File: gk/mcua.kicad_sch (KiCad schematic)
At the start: 16 parts, among them SW1 SW_Push, SW2 SW_Push, U4 STM32H747BITx, Y1 16MHz

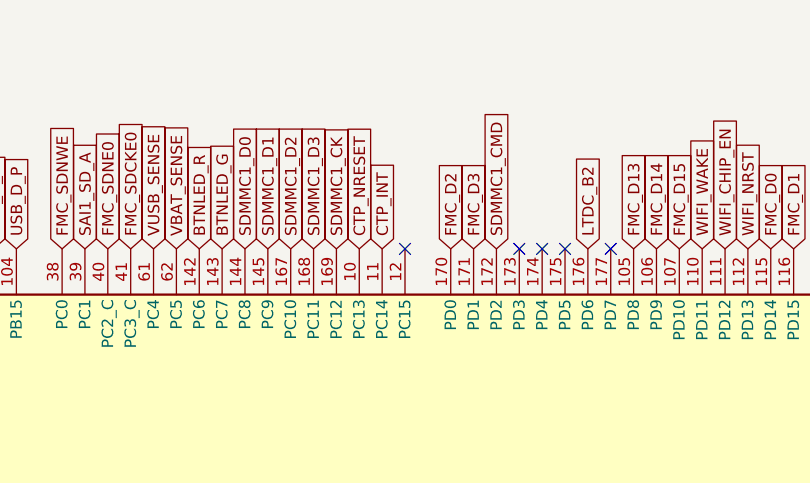
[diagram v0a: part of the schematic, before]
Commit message: Add SD power switch
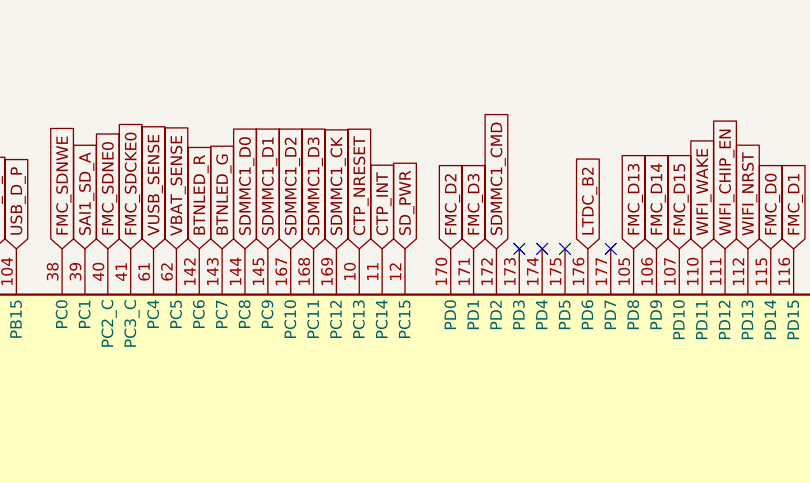
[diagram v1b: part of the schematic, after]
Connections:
- net SD_PWR: now reaches U4.12 (PC15)
- no-connect marks 20 -> 19
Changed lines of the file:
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@@
   (no_connect (at 66.04 49.53))
   (no_connect (at 35.56 49.53))
+  (no_connect (at 73.66 49.53))
   (no_connect (at 165.1 146.05))
   (no_connect (at 63.5 146.05))
   (no_connect (at 66.04 146.05))
   (no_connect (at 50.8 146.05))
-  (no_connect (at 160.02 49.53))
   (no_connect (at 86.36 146.05))
   (no_connect (at 73.66 146.05))
-  (no_connect (at 73.66 49.53))
   (no_connect (at 58.42 49.53))
   (no_connect (at 60.96 146.05))
@@
       (effects (font (size 1.27 1.27)) (justify left) hide)
     )
+  )
+  (global_label "SD_PWR" (shape input) (at 160.02 49.53 90) (fields_autoplaced)
+    (effects (font (size 1.27 1.27)) (justify left))
+    (property "Intersheetrefs" "${INTERSHEET_REFS}" (at 160.02 39.1063 90)
+      (effects (font (size 1.27 1.27)) (justify left) hide)
+    )

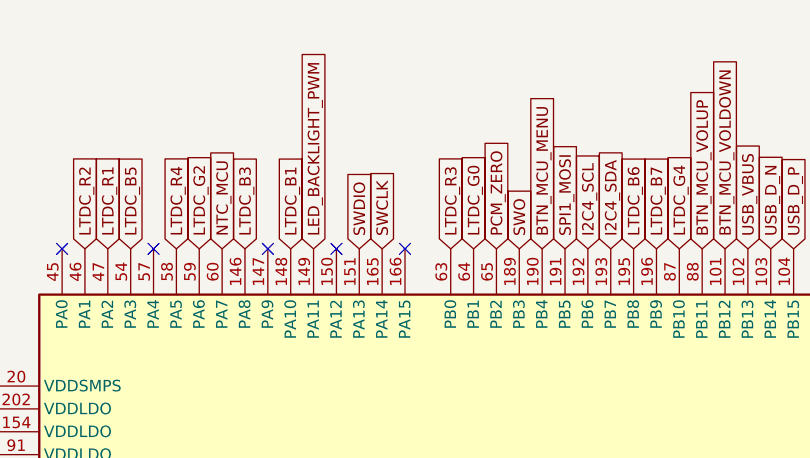
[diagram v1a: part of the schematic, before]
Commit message: update power button routing
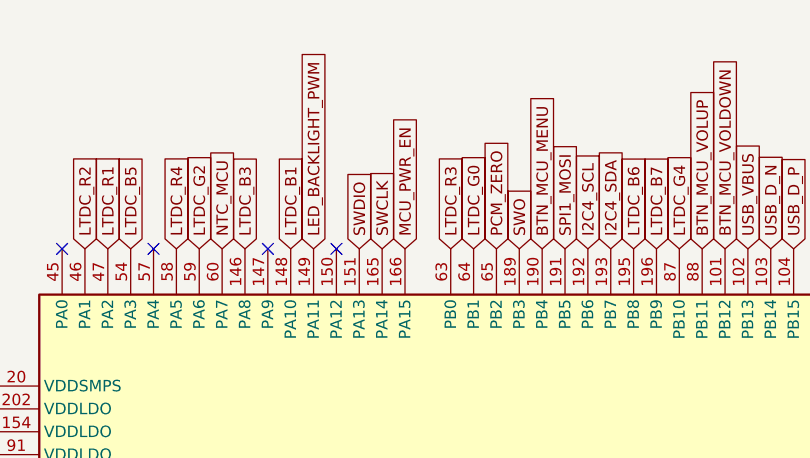
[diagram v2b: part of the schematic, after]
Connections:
- net MCU_PWR_EN: now reaches U4.166 (PA15)
- no-connect marks 19 -> 18
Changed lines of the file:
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@@
   (no_connect (at 66.04 49.53))
   (no_connect (at 35.56 49.53))
-  (no_connect (at 73.66 49.53))
   (no_connect (at 165.1 146.05))
   (no_connect (at 63.5 146.05))
@@
       (effects (font (size 1.27 1.27)) (justify left) hide)
     )
+  )
+  (global_label "MCU_PWR_EN" (shape input) (at 73.66 49.53 90) (fields_autoplaced)
+    (effects (font (size 1.27 1.27)) (justify left))
+    (property "Intersheetrefs" "${INTERSHEET_REFS}" (at 73.66 34.0868 90)
+      (effects (font (size 1.27 1.27)) (justify left) hide)
+    )

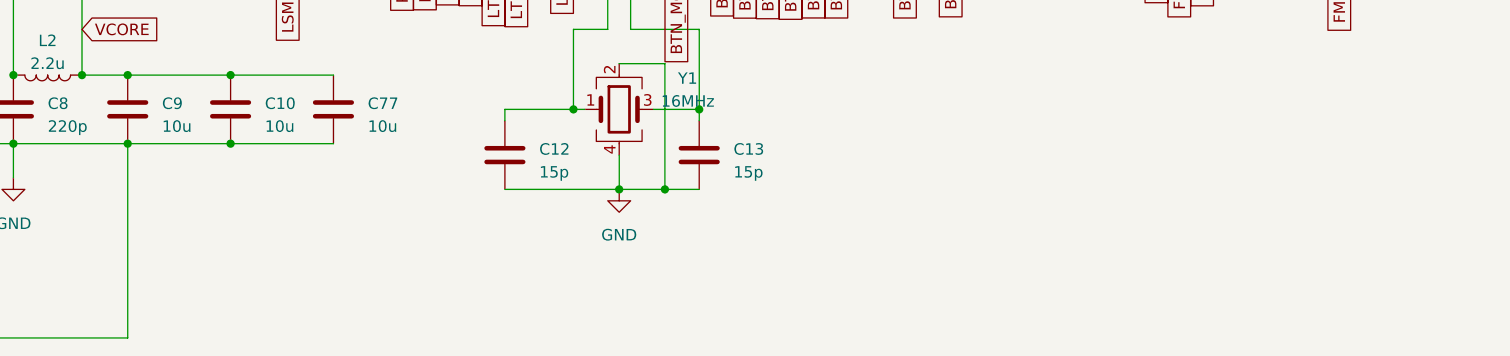
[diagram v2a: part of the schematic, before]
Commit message: add power supply TODOs to pcb
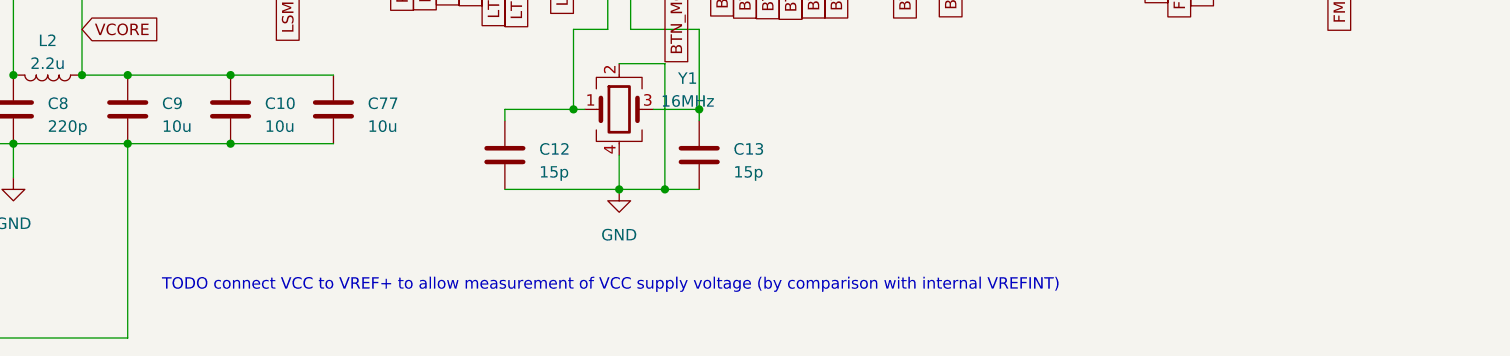
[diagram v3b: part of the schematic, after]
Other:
- note added: "TODO connect VCC to VREF+ to allow measurement of VCC supply voltage (by comparison with internal VREFINT)"
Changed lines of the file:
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@@
     (stroke (width 0) (type default))
+  )
+  (text "TODO connect VCC to VREF+ to allow measurement of VCC supply voltage (by comparison with internal VREFINT)"
+    (at 64.77 189.23 0)
+    (effects (font (size 1.27 1.27)) (justify left bottom))
   )
   (global_label "FMC_A11" (shape input) (at 160.02 146.05 270) (fields_autoplaced)
